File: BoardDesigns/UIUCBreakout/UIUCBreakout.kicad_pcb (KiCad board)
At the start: 4 copper layers, 48.3 x 48.3 mm, 10 parts, among them J3 Conn_01x17, J4 Conn_01x17, U1 AT25FF321A-SHN-B, U2 ADXL367BCCZ-RL7, U3 BMP585

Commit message: UIUCBreakout: add R1/C4, tighten design rules, regenerate 4-layer fab package
Adds the two parts the board was missing:

- R1 (10 R) in series in the BMP585 supply. This is the Bosch-required
  inrush limiter from BMP585 datasheet 6.2.5 Fig. 27, and it sits in the
  power path -- without it U3 is unpowered. Same role as R2 on
  BitPresTagBMP585.
- C4 (0.22 uF) on the ADXL367 VREG_OUT pin. Required, not optional:
  ADXL367 datasheet Table 9 note 1 asks for an external 0.2 uF.

Design rules were on loose defaults (min annular 0.05 mm, edge clearance
0.075 mm). Replaced with the real rule set: 0.1016 mm clearance and track,
0.3 mm copper-to-edge, 0.1524 mm via annular, and explicit via classes
(0.5048/0.2 and 0.61/0.3).

The previously committed jlcpcb/gerber/ set was a 2-layer plot of a
4-layer board -- no CuIn1/CuIn2. That was not cosmetic: J3.7 and J4.1
have no on-layer track and reach +3.3V only through the In1 plane, so
that set would have fabricated a board with no power. Both inner layers
are now present and committed.

Drops the 2026-08-20 production/ export, which predates R1 and C4 and so
carried a BOM and CPL that would have left both unplaced.

Verified against the committed state:

- DRC in place with --refill-zones: 0 violations, 0 unconnected
- Gerbers vs saved board: 114/114 track starts match on CuTop+CuBottom;
  CuIn1/CuIn2 carry real geometry (2863 / 2642 coordinates). Checked by
  geometry, not mtime -- the board is 3 min newer than the export because
  exporting marks it dirty.
- Drill reconciliation: 59 = 59 (0.2 mm x3, 0.3 mm x22 vias, 1.0 mm x34
  header pins; NPTH empty)
- U1 is AT25FF321A-SHN-B, the 208-mil wide EIAJ SOIC. Footprint
  SOIC-8_5.3x6.2mm_P1.27mm is KiCad's JEITA/EIAJ 08-001-BBA 208-mil
  pattern and LCSC C5591126 is package SOIC-8-208mil. Correct pairing;
  the 150-mil part is -SSHN-B / C7455378.

Co-Authored-By: Claude Opus 5 (1M context) <noreply@anthropic.com>
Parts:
- added C4: C, Capacitor_SMD:C_0603_1608Metric, F.Cu at (131.7, 91.6)
- added R1: 10, libraries:R_0603_1608Metric, F.Cu at (135.1, 108.5)
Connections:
- J4 pad 16: /LPS_PWR -> /LPS_PWR_IN
- U2 pad 9: unconnected-(U2-VREG_OUT-Pad9) -> Net-(U2-VREG_OUT)
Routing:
- net /LPS_PWR: track 37.4 -> 19.6 mm, vias 2 -> 3
- net /LPS_PWR_IN: track 0.00 -> 16.5 mm
- net Net-(U2-VREG_OUT): track 0.00 -> 2.08 mm
- net GND: track 8.84 -> 9.72 mm, vias 7 -> 8
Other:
- board text added: "Geoffrey Brown 95/2026"
- board text added: "UIUC Breakout V2"
- board text removed: "Geoffrey Brown 8/20/26"
- board text removed: "UIUC Breakout V1"

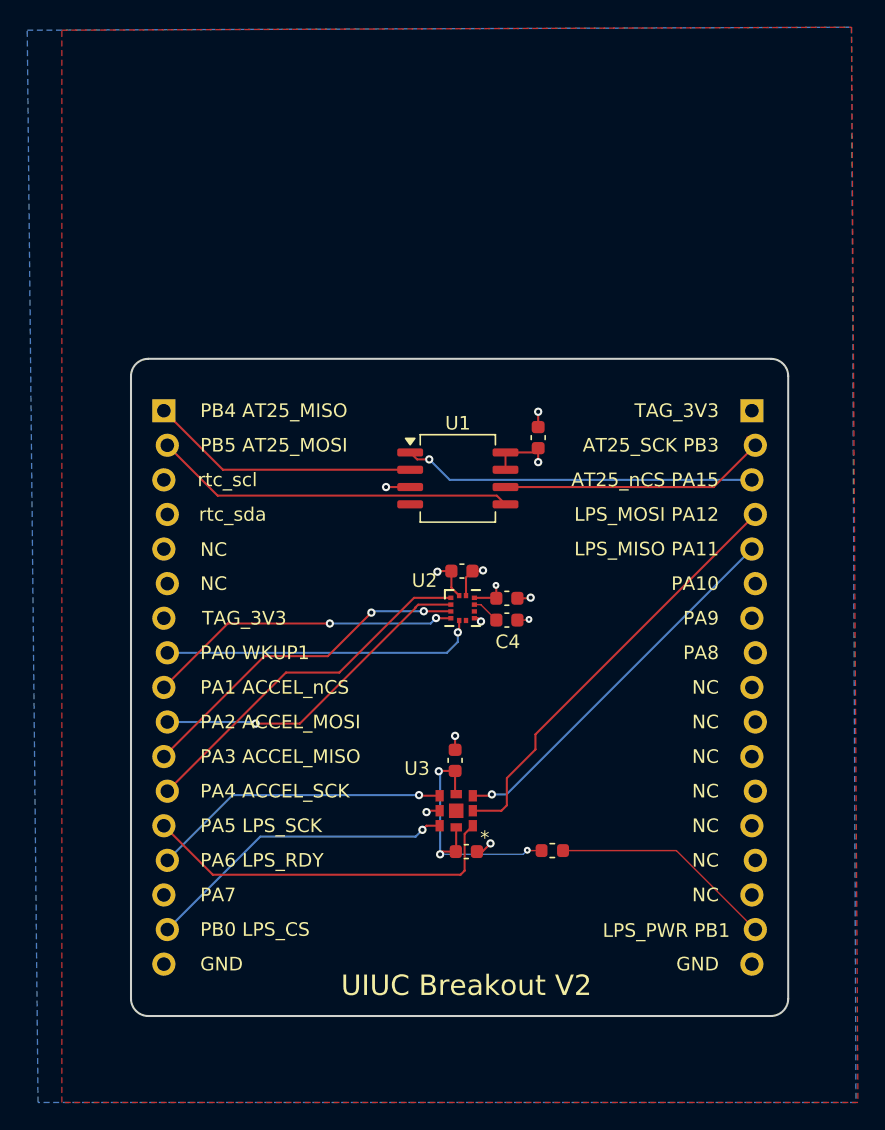
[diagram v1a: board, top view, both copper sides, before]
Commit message: UIUCBreakout: close out the review -- L1-L6 fixed, M3 accepted, L4 withdrawn
Board changes: C6 (4.7 uF) bulk added on +3.3V, 4.12 mm from U1.8; C4 Value
corrected to 0.22uf; U2 ADXL367 symbol refreshed from tag_library; PWR_FLAG
count 1 -> 3; silkscreen at J3.3/J3.4 relabelled PB7/PB6; back-silk date and
the J4.16 LPS_PWR_IN label corrected.

ERC goes from 8 violations to 2 warnings, 0 errors.

M3 -- accepted as-is, do not re-raise. U1 SIO2/SIO3 stay hard-tied to +3.3V
rather than pulled up. The tag has no room for the two resistors, and this
breakout is the preferred place for a quad-mode failure to happen: U1 here is
an 8-lead SOIC that can be desoldered and replaced by hand, where the tag's
WLCSP cannot. That is a better position than the review took -- it converts an
untestable hazard on the tag into a cheap, observable one here. The two
pin_to_pin ERC warnings on U1.3/U1.7 are therefore permanent and expected; they
are inherent to tying bidirectional pins to a net carrying a PWR_FLAG and
cannot be cleared by relocating the flag, since ERC evaluates net-wide.

L4 -- withdrawn, raised in error. The review claimed C7 sat 10.7 mm from the
flash it decouples. C7 is U2's cap, 1.61 mm from the ADXL367 VS pin; the flash
has C2 at 2.42 mm. Capacitors had been paired to parts by reading reference
designators instead of measuring. Measured nearest same-net cap per supply pin:
U1 VCC/C2 2.42, U2 VS/C7 1.61, U2 VDDIO/C1 1.89, U2 VREG_OUT/C4 1.97,
U3 VDD/C5 1.78, U3 VDDIO/C3 1.71 mm -- every supply pin within 2.73 mm. Only
the bulk half of the finding stood, and C6 addresses it.

L1 -- the baseboard fault is a WIRING error, not a naming error, and the
distinction decides the label. /stm32/rtc_scl really does carry the RV-3028's
SCL; what is crossed is which MCU pin it landed on (PB7, which is I2C1_SDA).
Checked against the Micro Crystal RV-3028-C7 Application Manual section 2.2
(pin 3 = SCL, pin 4 = SDA) rather than the KiCad symbol -- a mislabelled symbol
would have inverte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
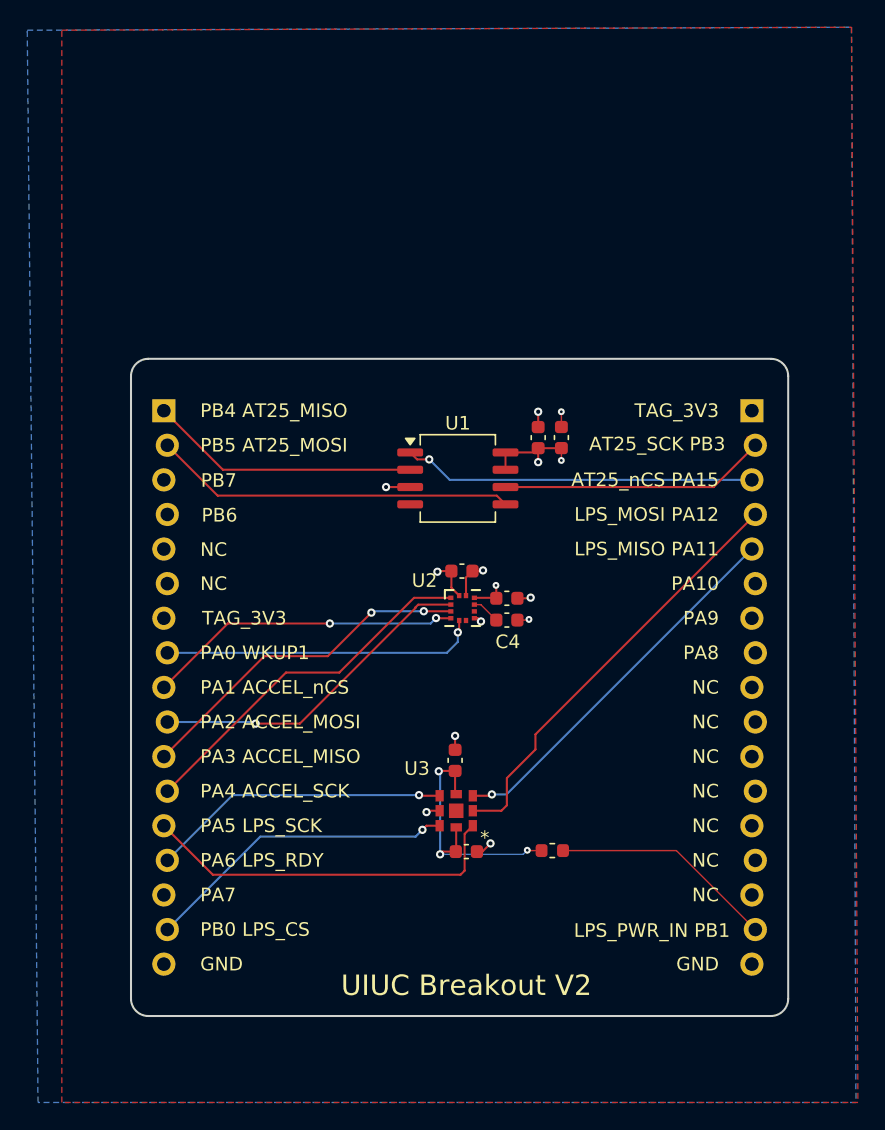
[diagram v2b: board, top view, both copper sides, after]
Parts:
- added C6: 4.7uf, Capacitor_SMD:C_0603_1608Metric, F.Cu at (135.7, 78.2)
- C4: value C -> 0.22uf
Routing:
- net +3.3V: track 12.3 -> 14.9 mm, vias 4 -> 5
- net GND: track 9.72 -> 10.8 mm, vias 8 -> 9
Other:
- board text added: "Geoffrey Brown 9/5/2026"
- board text added: "LPS_PWR_IN PB1"
- board text added: "PB6"
- board text added: "PB7"
- board text removed: "Geoffrey Brown 95/2026"
- board text removed: "LPS_PWR PB1"
- board text removed: "rtc_scl"
- board text removed: "rtc_sda"
